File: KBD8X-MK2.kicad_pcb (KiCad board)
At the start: 2 copper layers, 343.7 x 118.3 mm, 347 parts, among them J1 AVR-ISP-6, Q1 DSS60601MZ4-13, SW1 SW_Push, SW2 SW_SPDT, SW3 SW_SPDT, U1 ATmega32U4-MU, U2 PRTR5V0U2X, Y1 16MHz

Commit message: Fix PCB footprint mistake
There was a mistake with one of the footprints, which was not changed. All footprints are now Alps-compatible and the Gerber files have been updated.
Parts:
- D1, D10, D100, D101, D108, D11, D111, D112, D113, D12, D13, D14, D17, D18, D19, D2, D20, D21, D22, D23, D24, D25, D26, D27, D28, D29, D3, D30, D31, D35, D36, D37, D38, D39, D4, D40, D41, D42, D43, D44, D45, D46, D47, D48, D5, D52, D53, D54, D55, D56, D57, D58, D59, D6, D60, D61, D62, D63, D65, D66, D67, D68, D69, D7, D70, D71, D72, D73, D74, D75, D76, D77, D78, D8, D81, D82, D84, D85, D86, D87, D9, D90, D91, D92, D93, D94, D95, D96, D97, D99: value SOD-323 -> SOD-123
- SW_=1: renamed from MX_=1; value MX-1U -> 1U; footprint MX_Alps_Hybrid:MXOnly-1U -> MX_Alps_Hybrid:MX-1U
- U1: value ATmega32U4-MU -> ATmega32U4-AU; footprint locallib:QFN-44-1EP_7x7mm_Pitch0.5mm -> Package_QFP:TQFP-44_10x10mm_P0.8mm
- moved Y1 4.79 mm to (353.7, 106.7)
- moved C8 4.08 mm to (351.0, 102.2)
- moved RC4 3.75 mm to (332.2, 115.5)
- moved C4 3.45 mm to (355.5, 103.1)
- moved C6 3.41 mm to (331.3, 111.7)
- moved C3 3.35 mm to (355.5, 110.4)
- moved RC1 3.33 mm to (336.6, 93.0)
- moved RC2 3.33 mm to (338.6, 93.0)
- moved C2 3.10 mm to (341.5, 96.6)
- moved C7 3.08 mm to (344.7, 115.7)
- moved C5 2.49 mm to (336.0, 98.0)
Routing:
- net +5V: track 2712.9 -> 2730.7 mm
- net GND: track 1195.1 -> 1207.8 mm
- net ROW7: track 292.0 -> 299.4 mm
- net ROW9: track 317.4 -> 321.9 mm
- net ROW8: track 299.4 -> 303.2 mm
- net Net-(RC5-Pad1): track 31.4 -> 27.6 mm
- net RESET: track 53.7 -> 50.2 mm
- net RGBLED: track 103.4 -> 100.6 mm
- net ROW5: track 345.2 -> 347.9 mm
- net ROW4: track 388.3 -> 390.9 mm
- net COL0: track 559.6 -> 557.1 mm
- net ROW3: track 370.8 -> 373.3 mm
- net SLOCK_IND: track 105.7 -> 103.2 mm
- net Net-(RC2-Pad1): track 69.5 -> 67.0 mm
- net Net-(RC1-Pad2): track 67.5 -> 65.0 mm
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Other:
- rule pad_to_mask_clearance: 0.2 -> 0

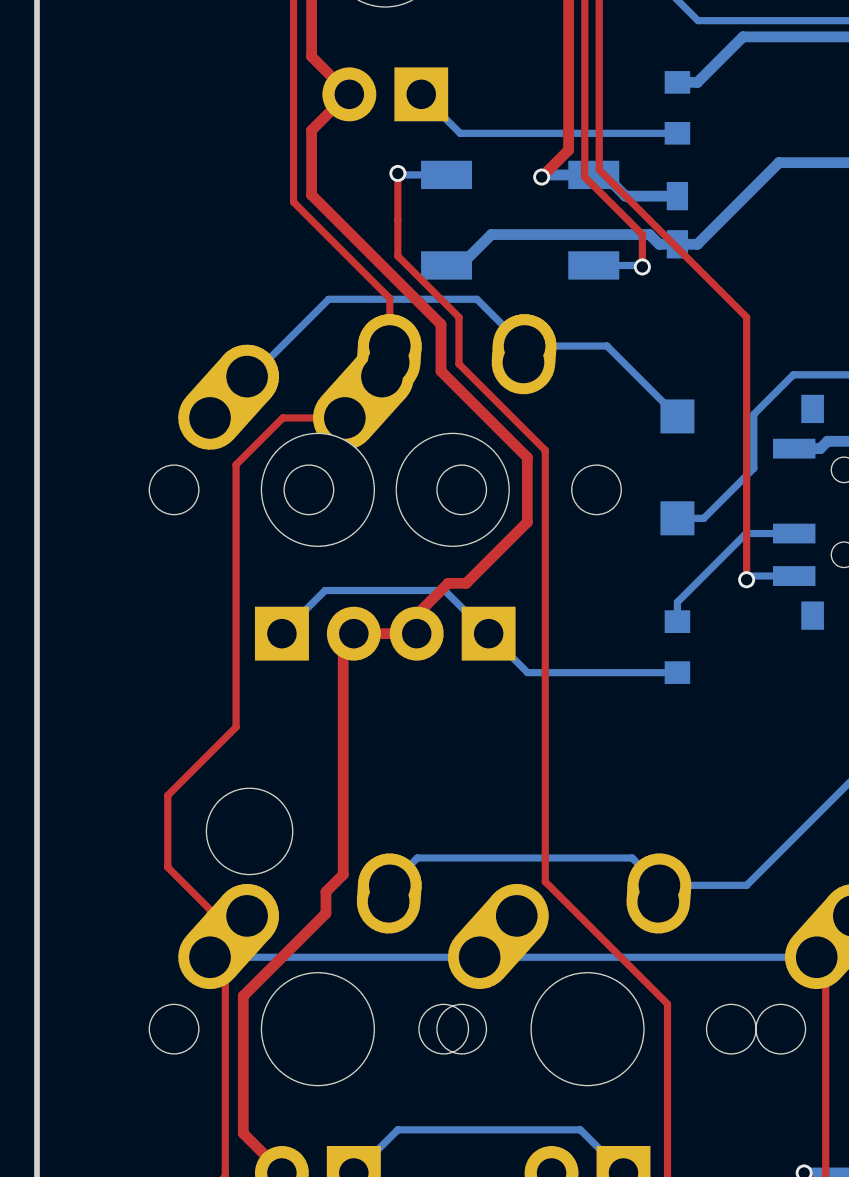
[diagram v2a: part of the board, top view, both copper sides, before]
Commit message: Updated for 3800 style Capslock
Added additional footprint for the 3800-style caps lock key. Gerbers updated as well.
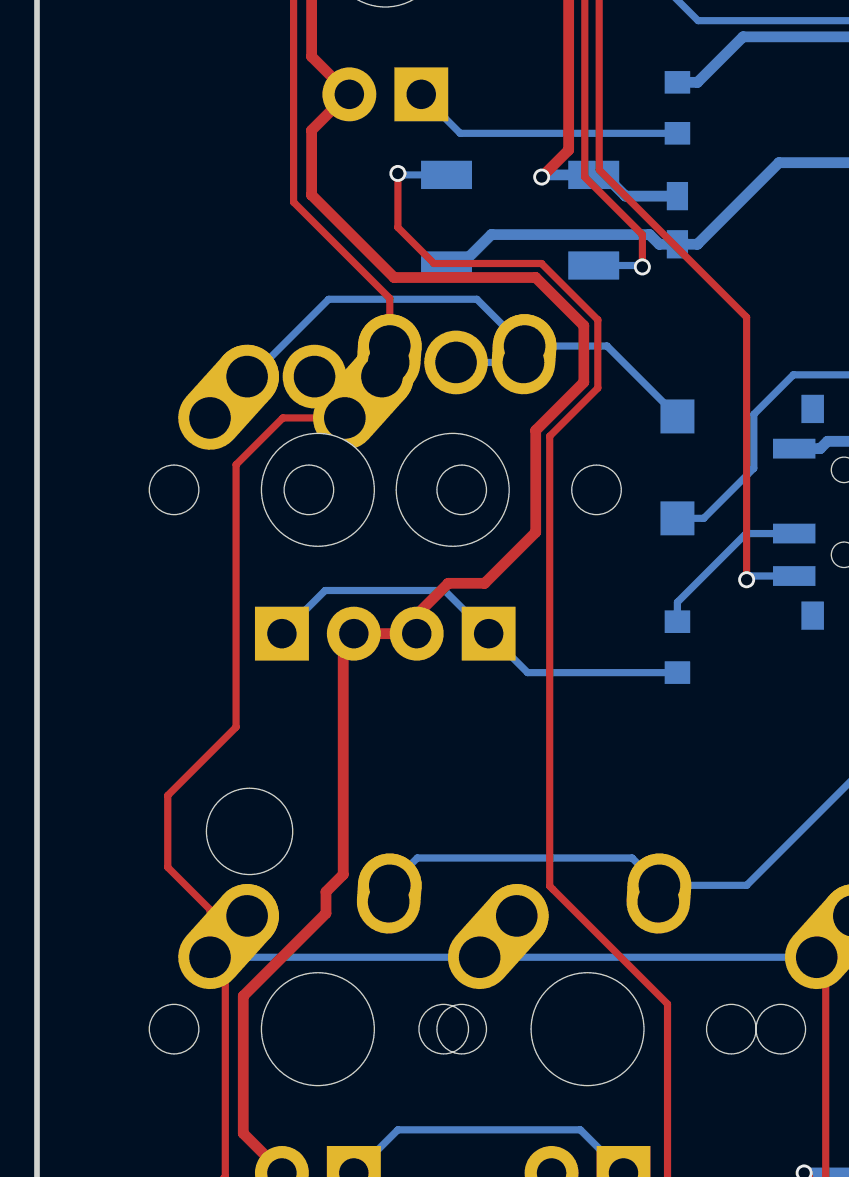
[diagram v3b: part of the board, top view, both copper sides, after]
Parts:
- added SW_CLOCK3800: 1.5U, MX_Alps_Hybrid:ALPS-1.5U, F.Cu at (52.4, 101.6)
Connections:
- SW_CLOCK2 pad 1: Net-(D52-Pad2) -> COL0
- SW_CLOCK2 pad 2: COL0 -> Net-(D52-Pad2)
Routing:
- net +5V: track 2730.7 -> 2735.7 mm
- net Net-(RGB10-Pad4): track 57.0 -> 60.6 mm
- net Net-(D52-Pad2): track 20.0 -> 22.3 mm

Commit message: Small silkscreen update
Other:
- board text added: "KBD8X-MKII Alps PCB Rev 2.12 2022-01-21"
- board text removed: "KBD8X-MKII PCB Rev 2.1 20211124"
